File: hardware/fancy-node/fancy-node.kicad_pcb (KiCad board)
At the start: 2 copper layers, 59.2 x 37 mm, 56 parts, among them J1 Conn_01x06, J2 Conn_01x02, J3 Conn_01x04, J4 USB_B_Micro, J5 Conn_01x03, SW1 SW_Push, SW2 SW_Push, SW3 SW_DPDT_x2, SW4 SW_Push, U1 CH340C, U2 STM32G030C8T6, U3 WS2812b, U5 HT75xx-1-SOT89, U6 RFM69CW-915MHZ, U7 TP4056

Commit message: fancy-node v1.0
Change-Id: I2dc287329bd6c7a9f578761cfc67db086f282b4b
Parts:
- added R6: 1k, Resistor_SMD:R_0402_1005Metric, F.Cu at (76.6, 71.8)
- added R7: 1k, Resistor_SMD:R_0402_1005Metric, F.Cu at (75.6, 69.5)
- added R8: 1k, Resistor_SMD:R_0402_1005Metric, F.Cu at (77.5, 69.5)
- J2: value Conn_01x02 -> Conn_01x03; footprint Connector_JST:JST_GH_SM02B-GHS-TB_1x02-1MP_P1.25mm_Horizontal -> Homebrew:MiniPV_78208-X03XXX_1x03_P2.54mm_Polarized_Horizontal; moved to B.Cu
- moved C12 14.0 mm to (34.8, 96.9), turned to -90 degrees
- moved H3 8.46 mm to (30.3, 98.0)
- moved C17 5.46 mm to (56.7, 87.7), turned to 90 degrees
- moved J2 5.44 mm to (29.1, 93.3), turned to 0 degrees
- moved C18 1.60 mm to (69.8, 92.8), turned to 90 degrees
- moved C10 1.50 mm to (45.5, 85.5)
- moved C19 1.05 mm to (42.8, 65.4)
- moved L1 1.03 mm to (41.0, 65.9)
- moved C3 0.80 mm to (56.9, 91.2)
- moved TH1 0.30 mm to (40.0, 92.2)
- moved D26 0.20 mm to (39.4, 87.8)
- moved C11 0.10 mm to (57.2, 84.6)
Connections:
- J1 pad 4: /AUX0 -> Net-(J1-Pad4)
- J1 pad 5: /AUX1 -> Net-(J1-Pad5)
- J1 pad 6: /AUX2 -> Net-(J1-Pad6)
- J2 pad 1: GND -> Net-(TH1-Pad2)
- J2 pad 2: Net-(TH1-Pad2) -> GND
- U2 pad 29: /AUX0 -> unconnected-(U2-Pad29)
- U2 pad 32: /AUX1 -> unconnected-(U2-Pad32)
- U2 pad 45: unconnected-(U2-Pad45) -> /AUX0
- U2 pad 46: unconnected-(U2-Pad46) -> /AUX1
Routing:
- net GND: track 0.00 -> 209.6 mm, vias 0 -> 58
- net /ANTENNA: track 0.00 -> 129.9 mm, vias 0 -> 19
- net +BATT: track 0.00 -> 120.8 mm, vias 0 -> 3
- net VCC: track 0.00 -> 118.2 mm, vias 0 -> 9
- net VBUS: track 0.00 -> 55.8 mm, vias 0 -> 3
- net /BATT_DIRECT: track 0.00 -> 34.1 mm, vias 0 -> 2
- net /EXTERNAL_LED: track 0.00 -> 31.2 mm, vias 0 -> 1
- net /~{DTR}: track 0.00 -> 30.2 mm, vias 0 -> 4
- net /MOSI: track 0.00 -> 26.6 mm, vias 0 -> 3
- net /USART_RX: track 0.00 -> 26.3 mm, vias 0 -> 2
- net /USART_TX: track 0.00 -> 25.7 mm, vias 0 -> 2
- net /SCK: track 0.00 -> 23.2 mm, vias 0 -> 3
- net /NSS: track 0.00 -> 20.7 mm, vias 0 -> 3
- net /DIO0: track 0.00 -> 18.9 mm, vias 0 -> 1
- net /~{STDBY}: track 0.00 -> 17.5 mm, vias 0 -> 2
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- added copper zone on B.Cu, net GND
- added copper zone on F.Cu, net GND
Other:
- board size 59.2 x 37 mm -> 60.2 x 37 mm
- board text added: "+"
- board text added: "+BAT"
- board text added: "-"
- board text added: "3V3"
- board text added: "AUX0"
- board text added: "AUX1"
- board text added: "AUX2"
- board text added: "CK"
- board text added: "D"
- board text added: "G"
- board text added: "GND"
- board text added: "IO"
- board text added: "OFF"
- board text added: "ON"
- board text added: "RESET"
- board text added: "SW1"
- board text added: "SW4"
- board text added: "VCC"
- board text added: "fancy-node v1.0"

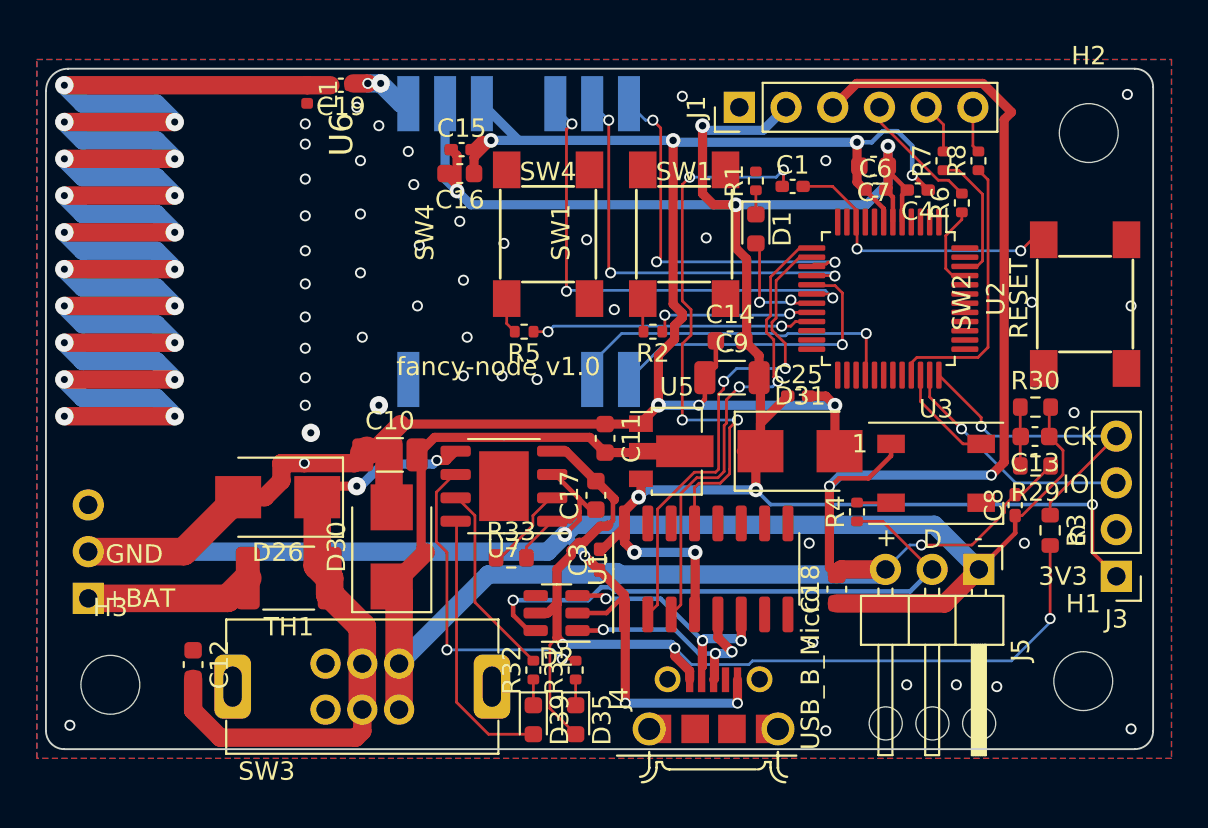
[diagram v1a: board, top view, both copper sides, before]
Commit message: fancy-node v1.1:
- Actually connect VBATT_DIV to micro
- Add resistor on DIO0 line to protect against firmware errors
- Move WS2812b line to SPI2, to not conflict with the radio SPI in case
we want to use the SPI with DMA to output the NRZ
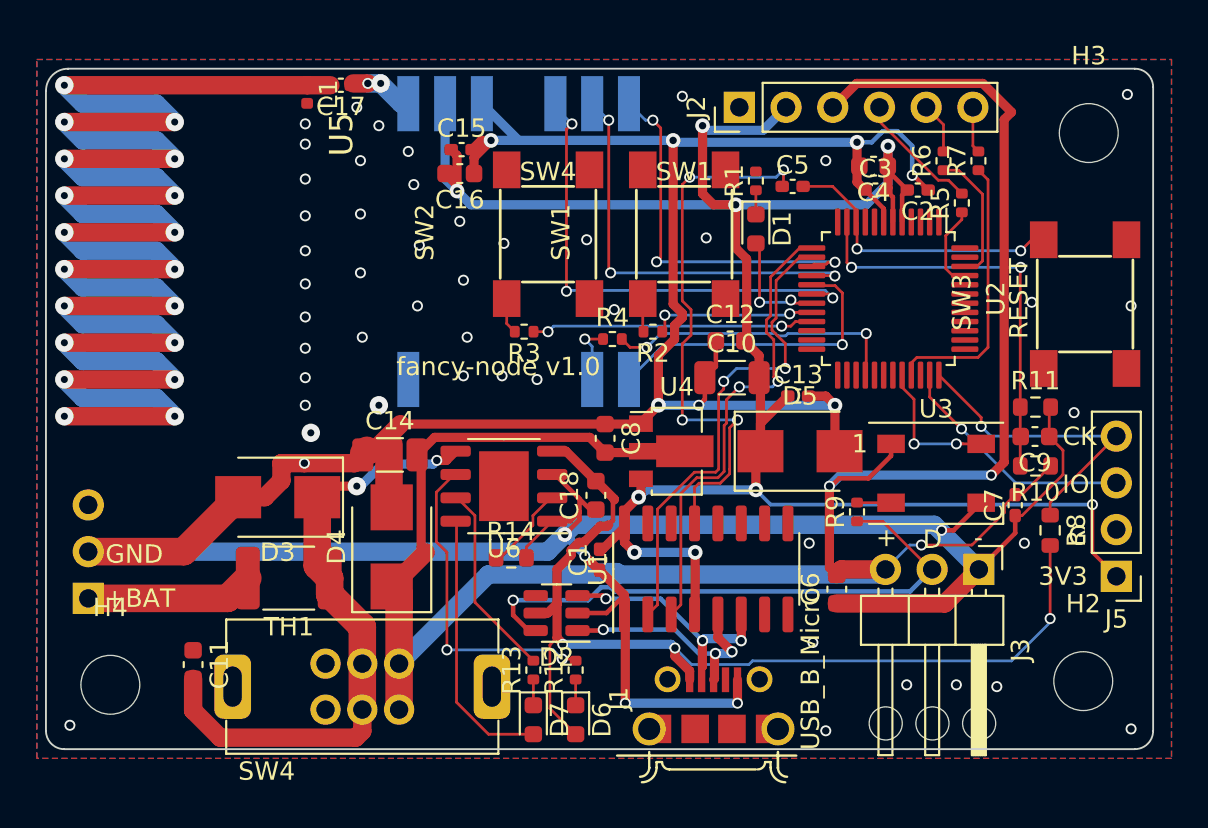
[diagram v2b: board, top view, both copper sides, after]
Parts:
- added R4: 1k, Resistor_SMD:R_0402_1005Metric, F.Cu at (57.6, 79.2)
- renumbered C3 to C1, C9 to C10, C12 to C11, C14 to C12, C25 to C13, C10 to C14, C19 to C17, C17 to C18, C4 to C2, C6 to C3, C7 to C4, C1 to C5, C18 to C6, C8 to C7, C11 to C8, C13 to C9, D26 to D3, D30 to D4, D31 to D5, D35 to D6, D39 to D7, H5 to H1, H1 to H2, H2 to H3, H3 to H4, J4 to J1, J1 to J2, J5 to J3, J2 to J4, J3 to J5, R29 to R10, R30 to R11, R31 to R12, R32 to R13, R33 to R14, R5 to R3, R6 to R5, R7 to R6, R8 to R7, R3 to R8, R4 to R9, SW4 to SW2, SW2 to SW3, SW3 to SW4, U5 to U4, U6 to U5, U7 to U6
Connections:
- U2 pad 11: unconnected-(U2-Pad11) -> /VBATT_DIV
- U2 pad 28: /DIO0 -> Net-(R4-Pad2)
- U2 pad 32: unconnected-(U2-Pad32) -> /INTERNAL_LED
- U2 pad 34: /INTERNAL_LED -> unconnected-(U2-Pad34)
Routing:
- net /VBATT_DIV: track 3.20 -> 22.6 mm, vias 0 -> 2
- net Net-(R4-Pad2): track 0.00 -> 16.2 mm, vias 0 -> 2
- net /DIO0: track 18.9 -> 3.35 mm
- net GND: track 209.6 -> 212.3 mm, vias 58 -> 59
- net /INTERNAL_LED: track 5.69 -> 7.66 mm, vias 0 -> 2
- net VCC: track 118.2 -> 116.5 mm

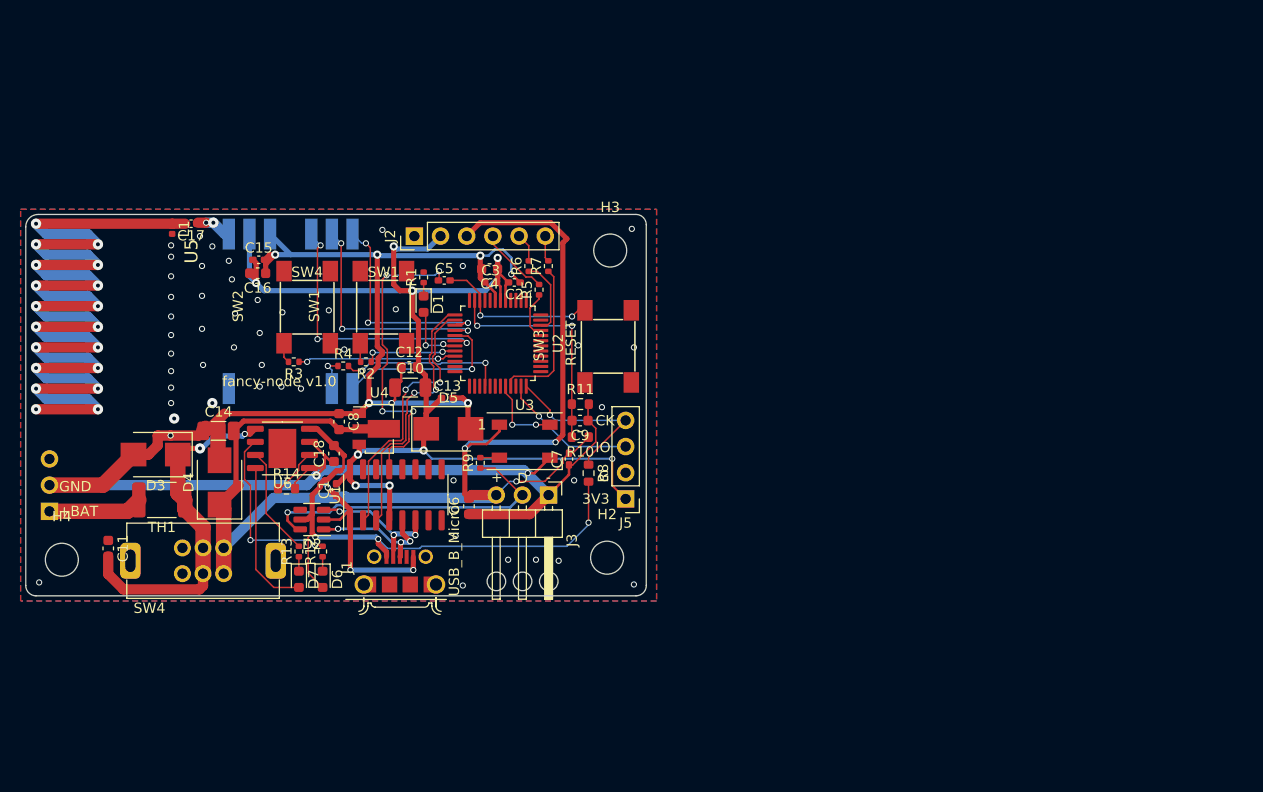
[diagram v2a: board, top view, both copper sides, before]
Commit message: Update schematic for fancy-node v1.2, and first pass at layout:
- Smaller buttons
- Smaller PCB antenna
- Smaller power switch
- Move to CH340X, hook up BOOT0 to it
- Smaller overall board size (47mm x 33mm, vs 60mm x 37mm)
- Add JST 1.25 for batteries
- Add crowbar diode for reverse polarity protection

Change-Id: I9a7a19972de9e62944e1a6f148661a5dd9e6b807
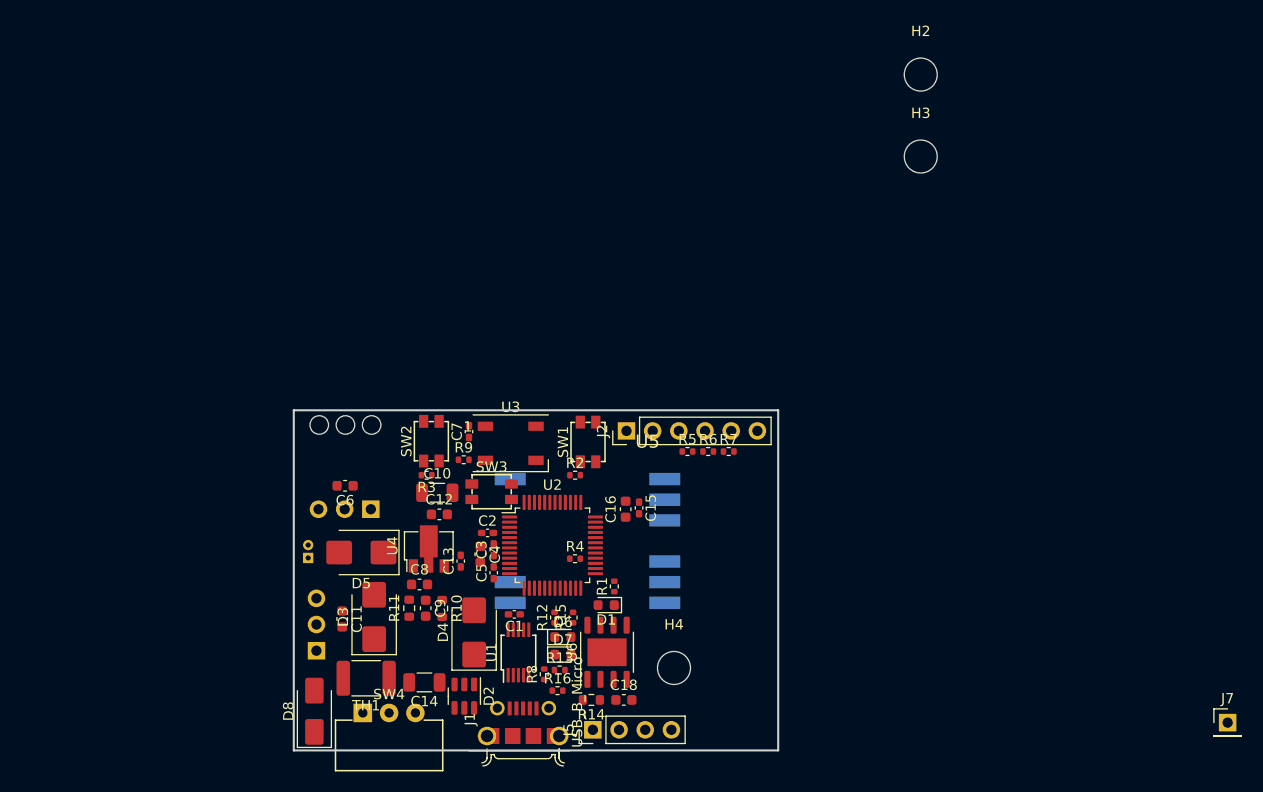
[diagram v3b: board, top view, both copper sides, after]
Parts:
- removed C17: 1pF, Capacitor_SMD:C_0402_1005Metric_Pad0.74x0.62mm_HandSolder
- removed L1: 10nH, Inductor_SMD:L_0402_1005Metric
- added D8: D, Diode_SMD:D_SMA, F.Cu at (54.8, 112.7)
- added J6: Conn_01x02, Homebrew:JST_Micro_1x02_P1.25mm_Horizontal, B.Cu at (54.2, 97.2)
- added J7: Conn_01x01, Connector_PinHeader_2.54mm:PinHeader_1x01_P2.54mm_Vertical, F.Cu at (143.4, 113.8)
- added R15: 1k, Resistor_SMD:R_0402_1005Metric, F.Cu at (79.9, 103.6)
- added R16: 4k7, Resistor_SMD:R_0402_1005Metric, F.Cu at (78.4, 110.7)
- D6: value GREEN -> WHITE
- J3: moved to B.Cu
- R8: value 3k3 -> 4k7; footprint Resistor_SMD:R_0603_1608Metric -> Resistor_SMD:R_0402_1005Metric
- SW1, SW2, SW3: footprint Homebrew:SW_TACTILE_5.1MM_TS-1187A-C-D-B -> Homebrew:SW_TACTILE_3mmx3.5mm_TS-1071SA-A4B3-D4
- SW4: value SW_DPDT_x2 -> SW_SPDT; footprint Homebrew:SK22D15L5_SP -> Homebrew:SW_SLIDE_SPDT_K3-1204D-L
- U1: value CH340C -> CH340X; footprint Package_SO:SOIC-16_3.9x9.9mm_P1.27mm -> Package_SO:MSOP-10_3x3mm_P0.5mm
- moved H4 60.3 mm to (89.7, 108.5)
- moved H2 55.9 mm to (113.6, 50.9)
- moved C15 44.1 mm to (86.3, 93.0), turned to -90 degrees
- moved C16 42.4 mm to (85.0, 93.1), turned to 90 degrees
- moved U6 37.2 mm to (83.2, 107.0), turned to 90 degrees
- moved C18 36.9 mm to (84.8, 111.6), turned to 0 degrees
- moved U5 36.4 mm to (81.3, 96.2), turned to 180 degrees
- moved R14 36.0 mm to (81.7, 111.6), turned to 180 degrees
- moved R1 35.2 mm to (83.9, 100.6)
- moved D1 34.1 mm to (83.1, 102.4), turned to 180 degrees
- moved C14 31.5 mm to (65.5, 109.9), turned to 180 degrees
- moved H3 31.5 mm to (113.6, 58.9)
- moved R4 29.2 mm to (80.1, 97.9)
- moved J4 29.2 mm to (55.0, 106.8)
- moved C5 28.8 mm to (72.2, 99.3), turned to 90 degrees
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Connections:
- D7 pad 2: Net-(D7-Pad2) -> VBUS
- R8 pad 1: /BOOT0 -> Net-(U1-~{CTS})
- R8 pad 2: VBUS -> /~{DTR}
- U1 pad 1: GND -> /USB+
- U1 pad 10: unconnected-(U1-Pad10) -> VCC
- U1 pad 2: /USART_RX -> /USB-
- U1 pad 3: /USART_TX -> GND
- U1 pad 4: VCC -> Net-(U1-~{RTS})
- U1 pad 5: /USB+ -> Net-(U1-~{CTS})
- U1 pad 6: /USB- -> /~{DTR}
- U1 pad 7: unconnected-(U1-Pad7) -> VCC
- U1 pad 8: unconnected-(U1-Pad8) -> /USART_RX
- U1 pad 9: unconnected-(U1-Pad9) -> /USART_TX
- U2 pad 11: /VBATT_DIV -> /AUX2
- U2 pad 12: unconnected-(U2-Pad12) -> /VBATT_DIV
- U2 pad 33: /AUX2 -> unconnected-(U2-PA11-Pad33)
- U5 pad 1: Net-(C17-Pad1) -> /ANTENNA
- U6 pad 8: Net-(D7-Pad2) -> Net-(U6-CE)
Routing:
- net GND: track 212.3 -> 0.00 mm, vias 59 -> 0
- net /ANTENNA: track 129.9 -> 0.00 mm, vias 19 -> 0
- net +BATT: track 120.8 -> 0.00 mm, vias 3 -> 0
- net VCC: track 116.5 -> 0.00 mm, vias 9 -> 0
- net VBUS: track 55.8 -> 0.00 mm, vias 3 -> 0
- net /BATT_DIRECT: track 34.1 -> 0.00 mm, vias 2 -> 0
- net /EXTERNAL_LED: track 31.2 -> 0.00 mm, vias 1 -> 0
- net /~{DTR}: track 30.2 -> 0.00 mm, vias 4 -> 0
- net /MOSI: track 26.6 -> 0.00 mm, vias 3 -> 0
- net /USART_RX: track 26.3 -> 0.00 mm, vias 2 -> 0
- net /USART_TX: track 25.7 -> 0.00 mm, vias 2 -> 0
- net /SCK: track 23.2 -> 0.00 mm, vias 3 -> 0
- net /VBATT_DIV: track 22.6 -> 0.00 mm, vias 2 -> 0
- net /NSS: track 20.7 -> 0.00 mm, vias 3 -> 0
- net /~{STDBY}: track 17.5 -> 0.00 mm, vias 2 -> 0
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- removed copper zone on B.Cu, net GND
- removed copper zone on F.Cu, net GND
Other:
- board size 60.2 x 37 mm -> 47 x 33 mm
- board text removed: "+"
- board text removed: "+BAT"
- board text removed: "-"
- board text removed: "3V3"
- board text removed: "AUX0"
- board text removed: "AUX1"
- board text removed: "AUX2"
- board text removed: "CK"
- board text removed: "D"
- board text removed: "G"
- board text removed: "GND"
- board text removed: "IO"
- board text removed: "OFF"
- board text removed: "ON"
- board text removed: "RESET"
- board text removed: "SW1"
- board text removed: "SW4"
- board text removed: "VCC"
- board text removed: "fancy-node v1.0"

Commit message: More fancy-node v1.2 changes
Change-Id: I98cb262bb1c5ca5a4a3b6f15447a12dbf8e0580a
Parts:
- removed J7: Conn_01x01, Connector_PinHeader_2.54mm:PinHeader_1x01_P2.54mm_Vertical
- added L1: 27nH, Inductor_SMD:L_0402_1005Metric, F.Cu at (96.9, 90.2)
- moved SW3 15.0 mm to (86.1, 96.6), turned to 180 degrees
- moved R5 9.53 mm to (82.9, 92.5)
- moved R6 9.16 mm to (84.3, 90.3)
- moved R7 9.15 mm to (86.3, 90.3)
- moved D8 6.62 mm to (60.7, 109.7), turned to 0 degrees
- moved TH1 6.16 mm to (54.9, 113.2), turned to -90 degrees
- moved R4 5.13 mm to (85.0, 99.4), turned to 90 degrees
- moved C6 2.58 mm to (57.7, 93.4)
- moved C7 2.40 mm to (69.8, 88.0)
- moved J2 2.40 mm to (85.1, 87.9)
- moved R9 2.40 mm to (69.3, 90.7)
- moved SW2 2.40 mm to (66.2, 88.9)
- moved SW1 2.40 mm to (81.3, 89.0)
- moved U3 2.40 mm to (73.8, 89.1)
- moved H1 2.28 mm to (57.8, 87.2)
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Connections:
- U5 pad 1: /ANTENNA -> Net-(U5-ANT)
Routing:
- net /ANTENNA: track 0.00 -> 26.3 mm
- net Net-(U5-ANT): track 0.00 -> 6.61 mm, vias 0 -> 1
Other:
- board size 47 x 33 mm -> 47.1 x 30.7 mm
